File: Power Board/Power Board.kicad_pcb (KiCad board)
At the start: 2 copper layers, 1 part

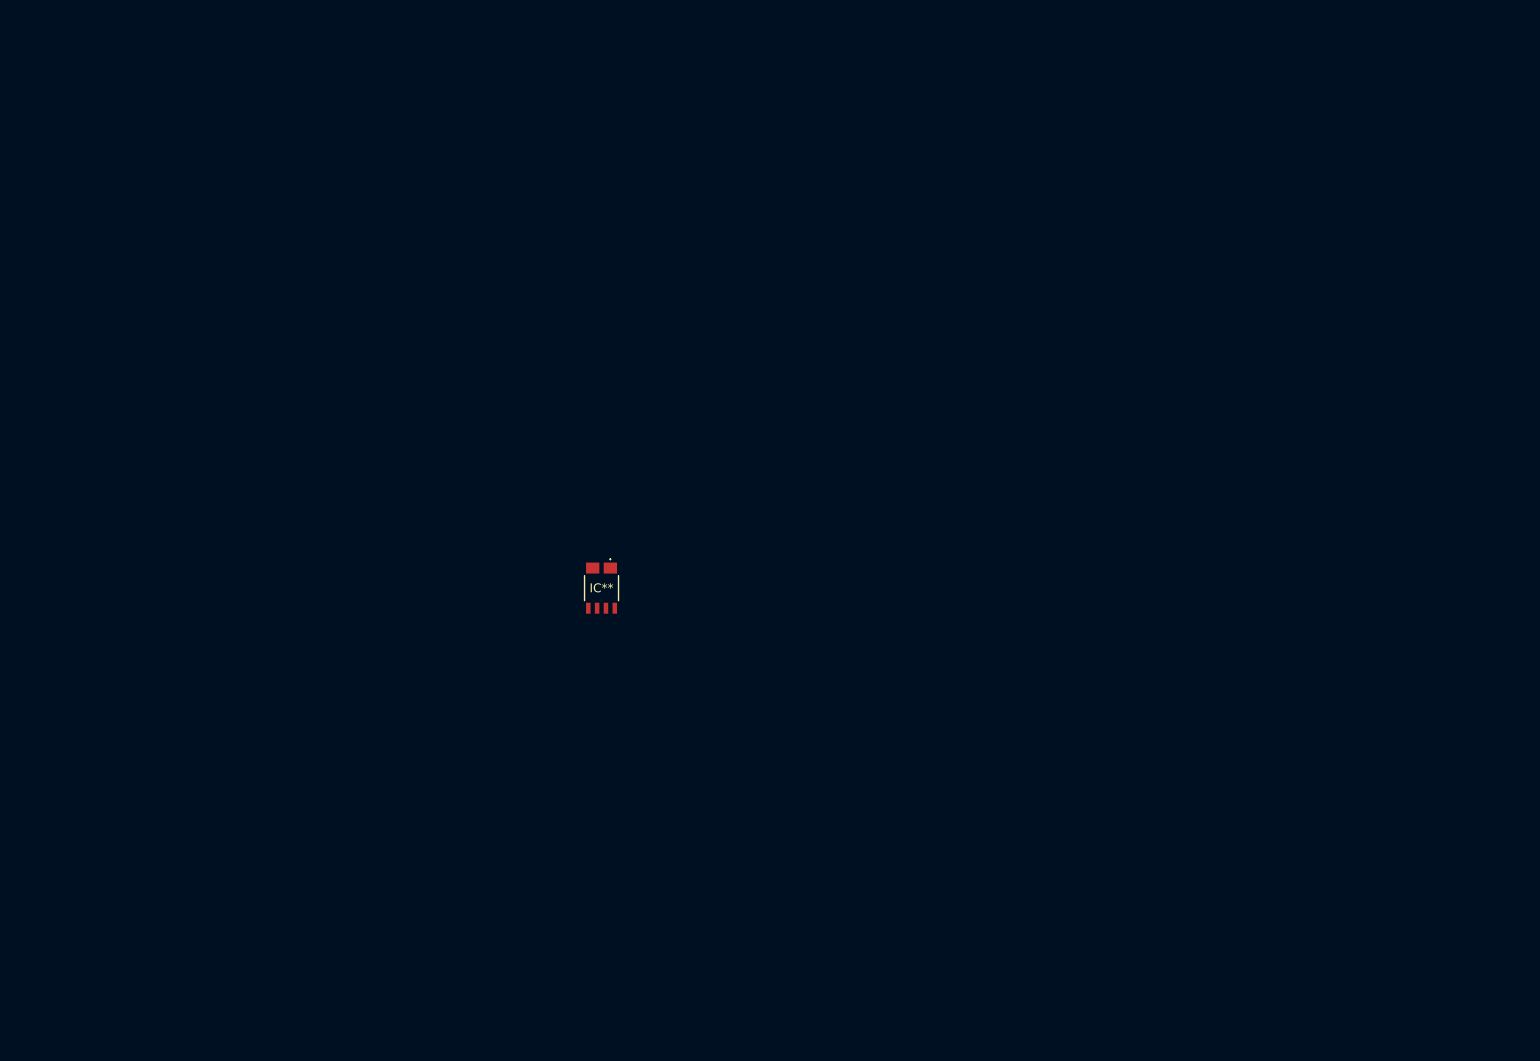
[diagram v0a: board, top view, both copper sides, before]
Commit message: power board update
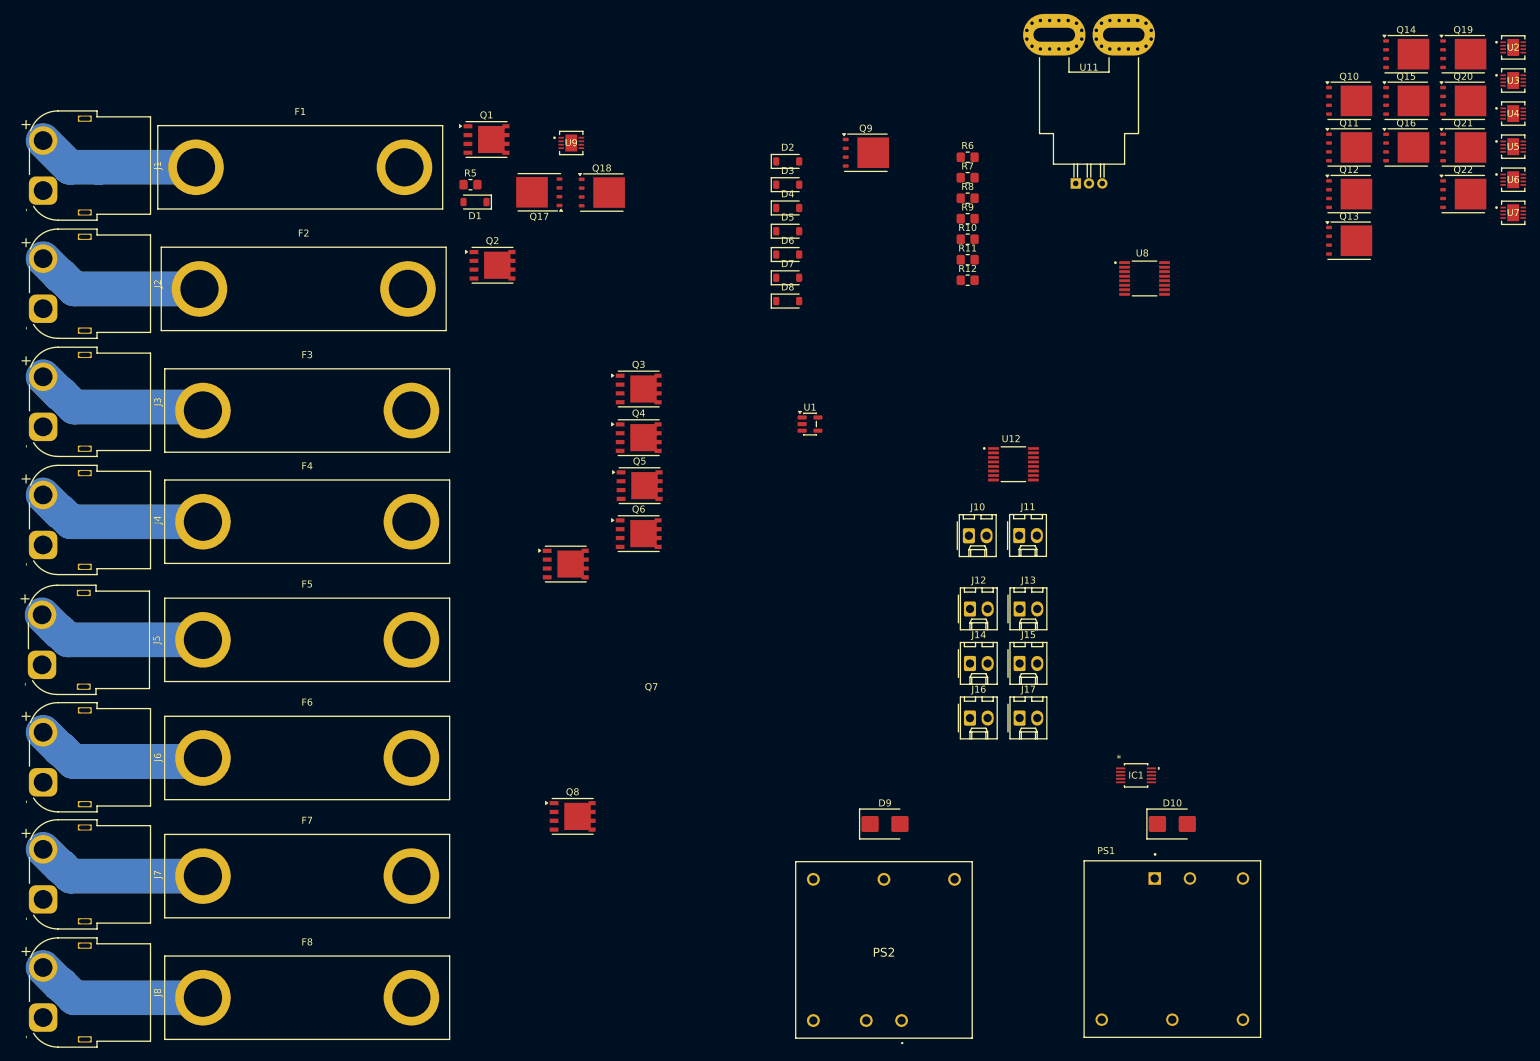
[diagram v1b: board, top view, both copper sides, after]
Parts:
- removed IC**: ACS37010LLZATR050B5, ACS37010LLZATR-050B5:ACS37010LLZATR050B5
- added D1: D_Zener, Diode_SMD:D_SOD-123, F.Cu at (131.7, 43.5)
- added D10: D_Zener, Diode_SMD:D_SMB, F.Cu at (232.0, 133.0)
- added D2: D_Zener, Diode_SMD:D_SOD-123, F.Cu at (176.7, 37.6)
- added D3: D_Zener, Diode_SMD:D_SOD-123, F.Cu at (176.7, 41.0)
- added D4: D_Zener, Diode_SMD:D_SOD-123, F.Cu at (176.7, 44.4)
- added D5: D_Zener, Diode_SMD:D_SOD-123, F.Cu at (176.7, 47.7)
- added D6: D_Zener, Diode_SMD:D_SOD-123, F.Cu at (176.7, 51.0)
- added D7: D_Zener, Diode_SMD:D_SOD-123, F.Cu at (176.7, 54.4)
- added D8: D_Zener, Diode_SMD:D_SOD-123, F.Cu at (176.7, 57.8)
- added D9: D_Zener, Diode_SMD:D_SMB, F.Cu at (190.7, 133.0)
- added F1: Fuse, 0498060:Fuse_0498060M, F.Cu at (106.5, 38.5)
- added F2: Fuse, 0498060:Fuse_0498060M, F.Cu at (107.0, 56.0)
- added F3: Fuse, 0498060:Fuse_0498060M, F.Cu at (107.5, 73.5)
- added F4: Fuse, 0498060:Fuse_0498060M, F.Cu at (107.5, 89.5)
- added F5: Fuse, 0498060:Fuse_0498060M, F.Cu at (107.5, 106.5)
- added F6: Fuse, 0498060:Fuse_0498060M, F.Cu at (107.5, 123.5)
- added F7: Fuse, 0498060:Fuse_0498060M, F.Cu at (107.5, 140.5)
- added F8: Fuse, 0498060:Fuse_0498060M, F.Cu at (107.5, 158.0)
- added IC1: LTC4151IMS#PBF, LTC4151:MSOP-10_MS_LIT, F.Cu at (226.8, 126.0)
- added J1: Conn_01x02, Connector_AMASS:AMASS_XT60PW-F_1x02_P7.20mm_Horizontal, F.Cu at (69.5, 41.9)
- added J10: Conn_01x02, Connector_Molex:Molex_KK-254_AE-6410-02A_1x02_P2.54mm_Vertical, F.Cu at (202.7, 91.5)
- added J11: Conn_01x02, Connector_Molex:Molex_KK-254_AE-6410-02A_1x02_P2.54mm_Vertical, F.Cu at (210.0, 91.5)
- added J12: Conn_01x02, Connector_Molex:Molex_KK-254_AE-6410-02A_1x02_P2.54mm_Vertical, F.Cu at (202.9, 102.1)
- added J13: Conn_01x02, Connector_Molex:Molex_KK-254_AE-6410-02A_1x02_P2.54mm_Vertical, F.Cu at (210.0, 102.1)
- added J14: Conn_01x02, Connector_Molex:Molex_KK-254_AE-6410-02A_1x02_P2.54mm_Vertical, F.Cu at (202.9, 109.9)
- added J15: Conn_01x02, Connector_Molex:Molex_KK-254_AE-6410-02A_1x02_P2.54mm_Vertical, F.Cu at (210.0, 109.9)
- added J16: Conn_01x02, Connector_Molex:Molex_KK-254_AE-6410-02A_1x02_P2.54mm_Vertical, F.Cu at (202.9, 117.8)
- added J17: Conn_01x02, Connector_Molex:Molex_KK-254_AE-6410-02A_1x02_P2.54mm_Vertical, F.Cu at (210.0, 117.8)
- added J2: Conn_01x02, Connector_AMASS:AMASS_XT60PW-F_1x02_P7.20mm_Horizontal, F.Cu at (69.5, 58.9)
- added J3: Conn_01x02, Connector_AMASS:AMASS_XT60PW-F_1x02_P7.20mm_Horizontal, F.Cu at (69.5, 75.8)
- added J4: Conn_01x02, Connector_AMASS:AMASS_XT60PW-F_1x02_P7.20mm_Horizontal, F.Cu at (69.5, 92.8)
- added J5: Conn_01x02, Connector_AMASS:AMASS_XT60PW-F_1x02_P7.20mm_Horizontal, F.Cu at (69.3, 110.1)
- added J6: Conn_01x02, Connector_AMASS:AMASS_XT60PW-F_1x02_P7.20mm_Horizontal, F.Cu at (69.5, 127.0)
- added J7: Conn_01x02, Connector_AMASS:AMASS_XT60PW-F_1x02_P7.20mm_Horizontal, F.Cu at (69.5, 143.8)
- added J8: Conn_01x02, Connector_AMASS:AMASS_XT60PW-F_1x02_P7.20mm_Horizontal, F.Cu at (69.5, 160.8)
- added PS1: THN_10-4815WIR, THN_10_4815WIR:CONV_THN_10-4815WIR, F.Cu at (232.0, 151.0)
- added PS2: JTK3024S05, JTK3024S05:JTK3024S05, F.Cu at (193.0, 161.3)
- added Q1: Q_PMOS_GDS, Package_SO:PowerPAK_SO-8_Single, F.Cu at (133.3, 34.5)
- added Q10: Q_NMOS_GDS, Package_TO_SOT_SMD:TDSON-8-1, F.Cu at (257.4, 28.9)
- added Q11: Q_NMOS_GDS, Package_TO_SOT_SMD:TDSON-8-1, F.Cu at (257.4, 35.6)
- added Q12: Q_NMOS_GDS, Package_TO_SOT_SMD:TDSON-8-1, F.Cu at (257.4, 42.4)
- added Q13: Q_NMOS_GDS, Package_TO_SOT_SMD:TDSON-8-1, F.Cu at (257.4, 49.1)
- added Q14: Q_NMOS_GDS, Package_TO_SOT_SMD:TDSON-8-1, F.Cu at (265.7, 22.2)
- added Q15: Q_NMOS_GDS, Package_TO_SOT_SMD:TDSON-8-1, F.Cu at (265.7, 28.9)
- added Q16: Q_NMOS_GDS, Package_TO_SOT_SMD:TDSON-8-1, F.Cu at (265.7, 35.6)
- added Q17: Q_NMOS_GDS, Package_TO_SOT_SMD:TDSON-8-1, F.Cu at (140.9, 42.1)
- added Q18: Q_NMOS_GDS, Package_TO_SOT_SMD:TDSON-8-1, F.Cu at (149.9, 42.1)
- added Q19: Q_NMOS_GDS, Package_TO_SOT_SMD:TDSON-8-1, F.Cu at (273.9, 22.2)
- added Q2: Q_PMOS_GDS, Package_SO:PowerPAK_SO-8_Single, F.Cu at (134.2, 52.6)
- added Q20: Q_NMOS_GDS, Package_TO_SOT_SMD:TDSON-8-1, F.Cu at (273.9, 28.9)
- added Q21: Q_NMOS_GDS, Package_TO_SOT_SMD:TDSON-8-1, F.Cu at (273.9, 35.6)
- added Q22: Q_NMOS_GDS, Package_TO_SOT_SMD:TDSON-8-1, F.Cu at (273.9, 42.4)
- added Q3: Q_PMOS_GDS, Package_SO:PowerPAK_SO-8_Single, F.Cu at (155.2, 70.4)
- added Q4: Q_PMOS_GDS, Package_SO:PowerPAK_SO-8_Single, F.Cu at (155.2, 77.4)
- added Q5: Q_PMOS_GDS, Package_SO:PowerPAK_SO-8_Single, F.Cu at (155.3, 84.3)
- added Q6: Q_PMOS_GDS, Package_SO:PowerPAK_SO-8_Single, F.Cu at (155.2, 91.2)
- added Q7: Q_PMOS_GDS, Package_SO:PowerPAK_SO-8_Single, F.Cu at (144.7, 95.6)
- added Q8: Q_PMOS_GDS, Package_SO:PowerPAK_SO-8_Single, F.Cu at (145.7, 131.9)
- added Q9: Q_NMOS_GDS, Package_TO_SOT_SMD:TDSON-8-1, F.Cu at (187.9, 36.4)
- added R10: 100k, Resistor_SMD:R_0805_2012Metric_Pad1.20x1.40mm_HandSolder, F.Cu at (202.5, 48.9)
- added R11: 100k, Resistor_SMD:R_0805_2012Metric_Pad1.20x1.40mm_HandSolder, F.Cu at (202.5, 51.8)
- added R12: 100k, Resistor_SMD:R_0805_2012Metric_Pad1.20x1.40mm_HandSolder, F.Cu at (202.5, 54.8)
- added R5: 100k, Resistor_SMD:R_0805_2012Metric_Pad1.20x1.40mm_HandSolder, F.Cu at (131.0, 41.0)
- added R6: 100k, Resistor_SMD:R_0805_2012Metric_Pad1.20x1.40mm_HandSolder, F.Cu at (202.5, 37.0)
- added R7: 100k, Resistor_SMD:R_0805_2012Metric_Pad1.20x1.40mm_HandSolder, F.Cu at (202.5, 40.0)
- added R8: 100k, Resistor_SMD:R_0805_2012Metric_Pad1.20x1.40mm_HandSolder, F.Cu at (202.5, 43.0)
- added R9: 100k, Resistor_SMD:R_0805_2012Metric_Pad1.20x1.40mm_HandSolder, F.Cu at (202.5, 45.9)
- added U1: TLV70033_SOT23-5, Package_TO_SOT_SMD:SOT-23-5, F.Cu at (179.9, 75.5)
- added U11: ACS770xCB-200U-PFF, Sensor_Current:Allegro_CB_PFF, F.Cu at (218.1, 40.8)
- added U12: ADC128S052CIMT, ADC128S052CIMT_NOPB:SOP65P640X120-16N, F.Cu at (209.1, 81.2)
- added U2: LTC4372CDD-PBF, footprints:05-08-1698_ADI, F.Cu at (281.1, 21.3)
- added U3: LTC4372CDD-PBF, footprints:05-08-1698_ADI, F.Cu at (281.1, 26.0)
- added U4: LTC4372CDD-PBF, footprints:05-08-1698_ADI, F.Cu at (281.1, 30.8)
- added U5: LTC4372CDD-PBF, footprints:05-08-1698_ADI, F.Cu at (281.1, 35.5)
- added U6: LTC4372CDD-PBF, footprints:05-08-1698_ADI, F.Cu at (281.1, 40.3)
- added U7: LTC4372CDD-PBF, footprints:05-08-1698_ADI, F.Cu at (281.1, 45.0)
- added U8: ADC128S052CIMT, ADC128S052CIMT_NOPB:SOP65P640X120-16N, F.Cu at (228.0, 54.5)
- added U9: LTC4372CDD-PBF, footprints:05-08-1698_ADI, F.Cu at (145.5, 35.0)
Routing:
- net Net-(J6-Pin_2): track 0.00 -> 24.9 mm
- net Net-(J8-Pin_2): track 0.00 -> 24.4 mm
- net Net-(J2-Pin_2): track 0.00 -> 24.3 mm
- net Net-(J7-Pin_2): track 0.00 -> 24.2 mm
- net Net-(J1-Pin_2): track 0.00 -> 24.1 mm
- net Net-(J3-Pin_2): track 0.00 -> 23.8 mm
- net Net-(J5-Pin_2): track 0.00 -> 23.6 mm
- net Net-(J4-Pin_2): track 0.00 -> 23.1 mm
- net Net-(Q1-D): track 0.00 -> 2.50 mm

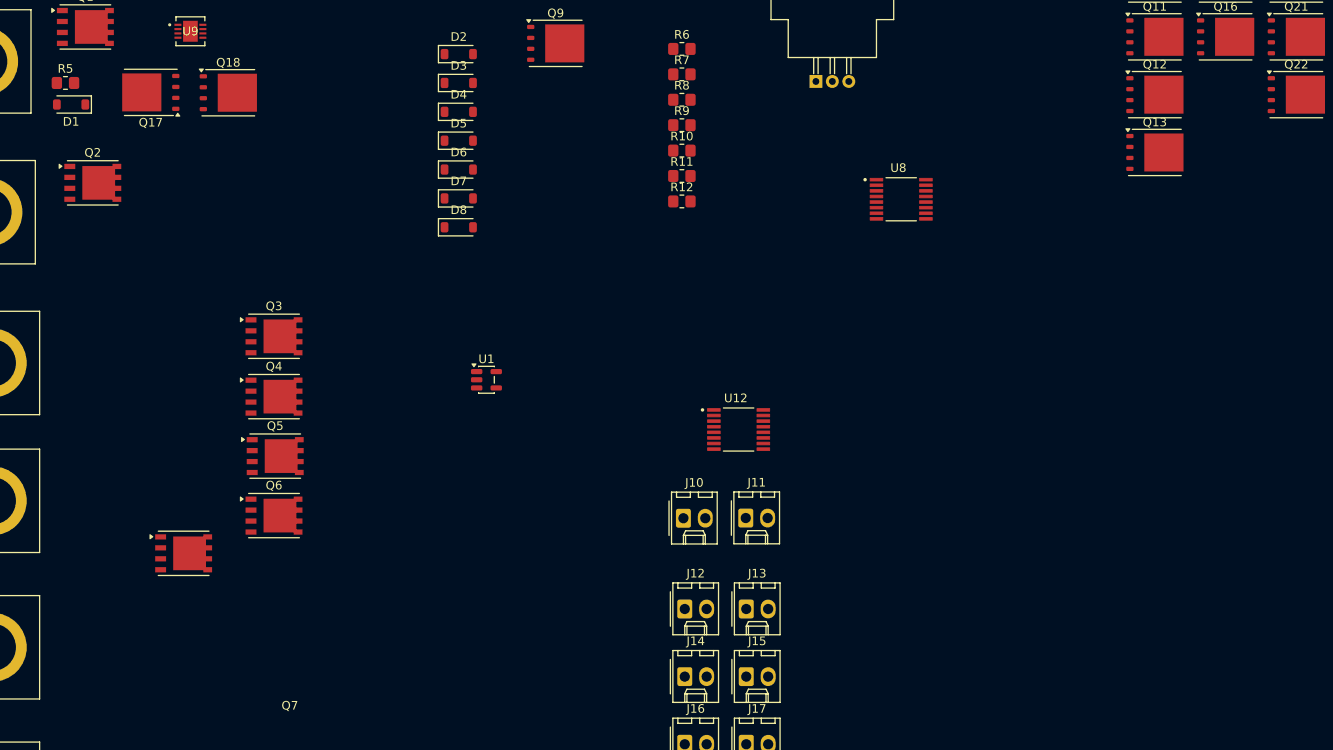
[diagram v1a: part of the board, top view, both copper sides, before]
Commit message: added resistor and capacitor footprints
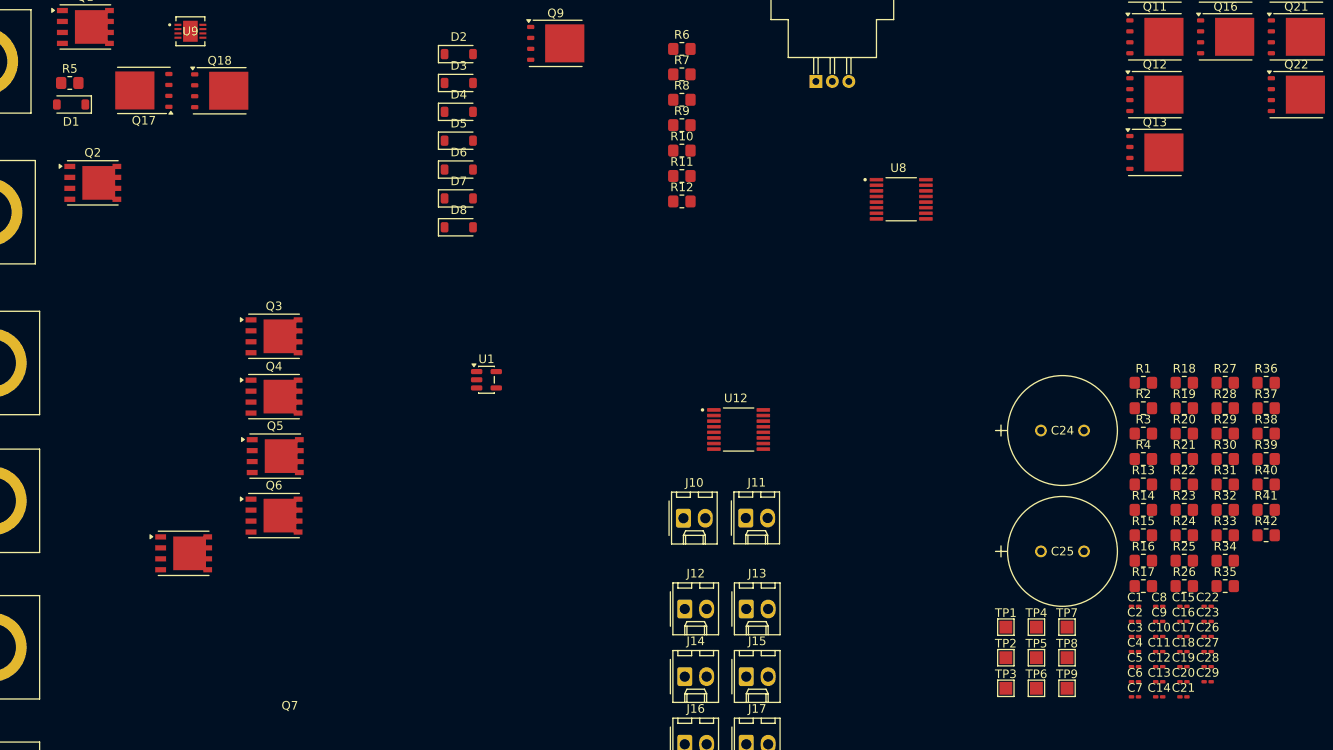
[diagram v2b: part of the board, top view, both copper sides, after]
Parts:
- added C1: 22 nF, Capacitor_SMD:C_0201_0603Metric_Pad0.64x0.40mm_HandSolder, F.Cu at (255.1, 101.8)
- added C10: 10 uF, Capacitor_SMD:C_0201_0603Metric_Pad0.64x0.40mm_HandSolder, F.Cu at (257.9, 105.2)
- added C11: 10nF, Capacitor_SMD:C_0201_0603Metric_Pad0.64x0.40mm_HandSolder, F.Cu at (257.9, 107.0)
- added C12: 100 nF, Capacitor_SMD:C_0201_0603Metric_Pad0.64x0.40mm_HandSolder, F.Cu at (257.9, 108.8)
- added C13: 100 nF, Capacitor_SMD:C_0201_0603Metric_Pad0.64x0.40mm_HandSolder, F.Cu at (257.9, 110.5)
- added C14: 100 nF, Capacitor_SMD:C_0201_0603Metric_Pad0.64x0.40mm_HandSolder, F.Cu at (257.9, 112.2)
- added C15: 100 nF, Capacitor_SMD:C_0201_0603Metric_Pad0.64x0.40mm_HandSolder, F.Cu at (260.8, 101.8)
- added C16: 10nF, Capacitor_SMD:C_0201_0603Metric_Pad0.64x0.40mm_HandSolder, F.Cu at (260.8, 103.5)
- added C17: 100 nF, Capacitor_SMD:C_0201_0603Metric_Pad0.64x0.40mm_HandSolder, F.Cu at (260.8, 105.2)
- added C18: 0.1 uF, Capacitor_SMD:C_0201_0603Metric_Pad0.64x0.40mm_HandSolder, F.Cu at (260.8, 107.0)
- added C19: 1 uF, Capacitor_SMD:C_0201_0603Metric_Pad0.64x0.40mm_HandSolder, F.Cu at (260.8, 108.8)
- added C2: 22 nF, Capacitor_SMD:C_0201_0603Metric_Pad0.64x0.40mm_HandSolder, F.Cu at (255.1, 103.5)
- added C20: 0.1 uF, Capacitor_SMD:C_0201_0603Metric_Pad0.64x0.40mm_HandSolder, F.Cu at (260.8, 110.5)
- added C21: 0.1 uF, Capacitor_SMD:C_0201_0603Metric_Pad0.64x0.40mm_HandSolder, F.Cu at (260.8, 112.2)
- added C22: 0.1 uF, Capacitor_SMD:C_0201_0603Metric_Pad0.64x0.40mm_HandSolder, F.Cu at (263.6, 101.8)
- added C23: 1 uF, Capacitor_SMD:C_0201_0603Metric_Pad0.64x0.40mm_HandSolder, F.Cu at (263.6, 103.5)
- added C24: UVZ2A331MHD1TO, UVZ2A331MHD:CAP_UEP_12P5X25_NCH, F.Cu at (244.2, 81.3)
- added C25: UVZ2A331MHD1TO, UVZ2A331MHD:CAP_UEP_12P5X25_NCH, F.Cu at (244.2, 95.4)
- added C26: 0.1 uF, Capacitor_SMD:C_0201_0603Metric_Pad0.64x0.40mm_HandSolder, F.Cu at (263.6, 105.2)
- added C27: 1 uF, Capacitor_SMD:C_0201_0603Metric_Pad0.64x0.40mm_HandSolder, F.Cu at (263.6, 107.0)
- added C28: 1uF, Capacitor_SMD:C_0201_0603Metric_Pad0.64x0.40mm_HandSolder, F.Cu at (263.6, 108.8)
- added C29: 1uF, Capacitor_SMD:C_0201_0603Metric_Pad0.64x0.40mm_HandSolder, F.Cu at (263.6, 110.5)
- added C3: 10nF, Capacitor_SMD:C_0201_0603Metric_Pad0.64x0.40mm_HandSolder, F.Cu at (255.1, 105.2)
- added C4: 100 nF, Capacitor_SMD:C_0201_0603Metric_Pad0.64x0.40mm_HandSolder, F.Cu at (255.1, 107.0)
- added C5: 10nF, Capacitor_SMD:C_0201_0603Metric_Pad0.64x0.40mm_HandSolder, F.Cu at (255.1, 108.8)
- added C6: 100 nF, Capacitor_SMD:C_0201_0603Metric_Pad0.64x0.40mm_HandSolder, F.Cu at (255.1, 110.5)
- added C7: 10nF, Capacitor_SMD:C_0201_0603Metric_Pad0.64x0.40mm_HandSolder, F.Cu at (255.1, 112.2)
- added C8: 10nF, Capacitor_SMD:C_0201_0603Metric_Pad0.64x0.40mm_HandSolder, F.Cu at (257.9, 101.8)
- added C9: 10nF, Capacitor_SMD:C_0201_0603Metric_Pad0.64x0.40mm_HandSolder, F.Cu at (257.9, 103.5)
- added R1: 0.04, Resistor_SMD:R_0805_2012Metric_Pad1.20x1.40mm_HandSolder, F.Cu at (256.1, 75.8)
- added R13: 10, Resistor_SMD:R_0805_2012Metric_Pad1.20x1.40mm_HandSolder, F.Cu at (256.1, 87.6)
- added R14: 1K, Resistor_SMD:R_0805_2012Metric_Pad1.20x1.40mm_HandSolder, F.Cu at (256.1, 90.5)
- added R15: 100, Resistor_SMD:R_0805_2012Metric_Pad1.20x1.40mm_HandSolder, F.Cu at (256.1, 93.5)
- added R16: 10, Resistor_SMD:R_0805_2012Metric_Pad1.20x1.40mm_HandSolder, F.Cu at (256.1, 96.5)
- added R17: 1K, Resistor_SMD:R_0805_2012Metric_Pad1.20x1.40mm_HandSolder, F.Cu at (256.1, 99.4)
- added R18: 100, Resistor_SMD:R_0805_2012Metric_Pad1.20x1.40mm_HandSolder, F.Cu at (260.9, 75.8)
- added R19: 10, Resistor_SMD:R_0805_2012Metric_Pad1.20x1.40mm_HandSolder, F.Cu at (260.9, 78.8)
- added R2: 100, Resistor_SMD:R_0805_2012Metric_Pad1.20x1.40mm_HandSolder, F.Cu at (256.1, 78.8)
- added R20: 10, Resistor_SMD:R_0805_2012Metric_Pad1.20x1.40mm_HandSolder, F.Cu at (260.9, 81.7)
- added R21: 1K, Resistor_SMD:R_0805_2012Metric_Pad1.20x1.40mm_HandSolder, F.Cu at (260.9, 84.7)
- added R22: 100, Resistor_SMD:R_0805_2012Metric_Pad1.20x1.40mm_HandSolder, F.Cu at (260.9, 87.6)
- added R23: 10, Resistor_SMD:R_0805_2012Metric_Pad1.20x1.40mm_HandSolder, F.Cu at (260.9, 90.5)
- added R24: 10, Resistor_SMD:R_0805_2012Metric_Pad1.20x1.40mm_HandSolder, F.Cu at (260.9, 93.5)
- added R25: 1K, Resistor_SMD:R_0805_2012Metric_Pad1.20x1.40mm_HandSolder, F.Cu at (260.9, 96.5)
- added R26: 1K, Resistor_SMD:R_0805_2012Metric_Pad1.20x1.40mm_HandSolder, F.Cu at (260.9, 99.4)
- added R27: 1K, Resistor_SMD:R_0805_2012Metric_Pad1.20x1.40mm_HandSolder, F.Cu at (265.6, 75.8)
- added R28: 100, Resistor_SMD:R_0805_2012Metric_Pad1.20x1.40mm_HandSolder, F.Cu at (265.6, 78.8)
- added R29: 100, Resistor_SMD:R_0805_2012Metric_Pad1.20x1.40mm_HandSolder, F.Cu at (265.6, 81.7)
- added R3: 100, Resistor_SMD:R_0805_2012Metric_Pad1.20x1.40mm_HandSolder, F.Cu at (256.1, 81.7)
- added R30: 100, Resistor_SMD:R_0805_2012Metric_Pad1.20x1.40mm_HandSolder, F.Cu at (265.6, 84.7)
- added R31: 10, Resistor_SMD:R_0805_2012Metric_Pad1.20x1.40mm_HandSolder, F.Cu at (265.6, 87.6)
- added R32: 1K, Resistor_SMD:R_0805_2012Metric_Pad1.20x1.40mm_HandSolder, F.Cu at (265.6, 90.5)
- added R33: 100, Resistor_SMD:R_0805_2012Metric_Pad1.20x1.40mm_HandSolder, F.Cu at (265.6, 93.5)
- added R34: 20k, Resistor_SMD:R_0805_2012Metric_Pad1.20x1.40mm_HandSolder, F.Cu at (265.6, 96.5)
- added R35: 10k, Resistor_SMD:R_0805_2012Metric_Pad1.20x1.40mm_HandSolder, F.Cu at (265.6, 99.4)
- added R36: 2.7K, Resistor_SMD:R_0805_2012Metric_Pad1.20x1.40mm_HandSolder, F.Cu at (270.4, 75.8)
- added R37: 2.7K, Resistor_SMD:R_0805_2012Metric_Pad1.20x1.40mm_HandSolder, F.Cu at (270.4, 78.8)
- added R38: 2.7K, Resistor_SMD:R_0805_2012Metric_Pad1.20x1.40mm_HandSolder, F.Cu at (270.4, 81.7)
- added R39: 2.7K, Resistor_SMD:R_0805_2012Metric_Pad1.20x1.40mm_HandSolder, F.Cu at (270.4, 84.7)
- added R4: 2.7K, Resistor_SMD:R_0805_2012Metric_Pad1.20x1.40mm_HandSolder, F.Cu at (256.1, 84.7)
- added R40: 2.7K, Resistor_SMD:R_0805_2012Metric_Pad1.20x1.40mm_HandSolder, F.Cu at (270.4, 87.6)
- added R41: 2.7K, Resistor_SMD:R_0805_2012Metric_Pad1.20x1.40mm_HandSolder, F.Cu at (270.4, 90.5)
- added R42: 2.7K, Resistor_SMD:R_0805_2012Metric_Pad1.20x1.40mm_HandSolder, F.Cu at (270.4, 93.5)
- added TP1: TestPoint, TestPoint:TestPoint_Pad_1.5x1.5mm, F.Cu at (240.1, 104.2)
- added TP2: TestPoint, TestPoint:TestPoint_Pad_1.5x1.5mm, F.Cu at (240.1, 107.7)
- added TP3: TestPoint, TestPoint:TestPoint_Pad_1.5x1.5mm, F.Cu at (240.1, 111.3)
- added TP4: TestPoint, TestPoint:TestPoint_Pad_1.5x1.5mm, F.Cu at (243.7, 104.2)
- added TP5: TestPoint, TestPoint:TestPoint_Pad_1.5x1.5mm, F.Cu at (243.7, 107.7)
- added TP6: TestPoint, TestPoint:TestPoint_Pad_1.5x1.5mm, F.Cu at (243.7, 111.3)
- added TP7: TestPoint, TestPoint:TestPoint_Pad_1.5x1.5mm, F.Cu at (247.2, 104.2)
- added TP8: TestPoint, TestPoint:TestPoint_Pad_1.5x1.5mm, F.Cu at (247.2, 107.7)
- added TP9: TestPoint, TestPoint:TestPoint_Pad_1.5x1.5mm, F.Cu at (247.2, 111.3)
- moved Q18 1.03 mm to (148.9, 41.9)
- moved Q17 0.84 mm to (140.1, 41.9)
- moved R5 0.50 mm to (131.5, 41.0)
